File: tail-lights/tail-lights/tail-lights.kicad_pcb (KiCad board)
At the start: 2 copper layers, 145 x 115 mm, 106 parts, among them IC1 ATMEGA328P-AU, IC2 NCV8402ASTT1G, IC3 NCV8402ASTT1G, IC4 NCV8402ASTT1G, IC5 TPS62160DGKR, J1 Conn_01x01, J2 Conn_01x01, J3 Conn_01x06_Female, J4 Conn_01x04_Female, Y1 X322516MLB4SI

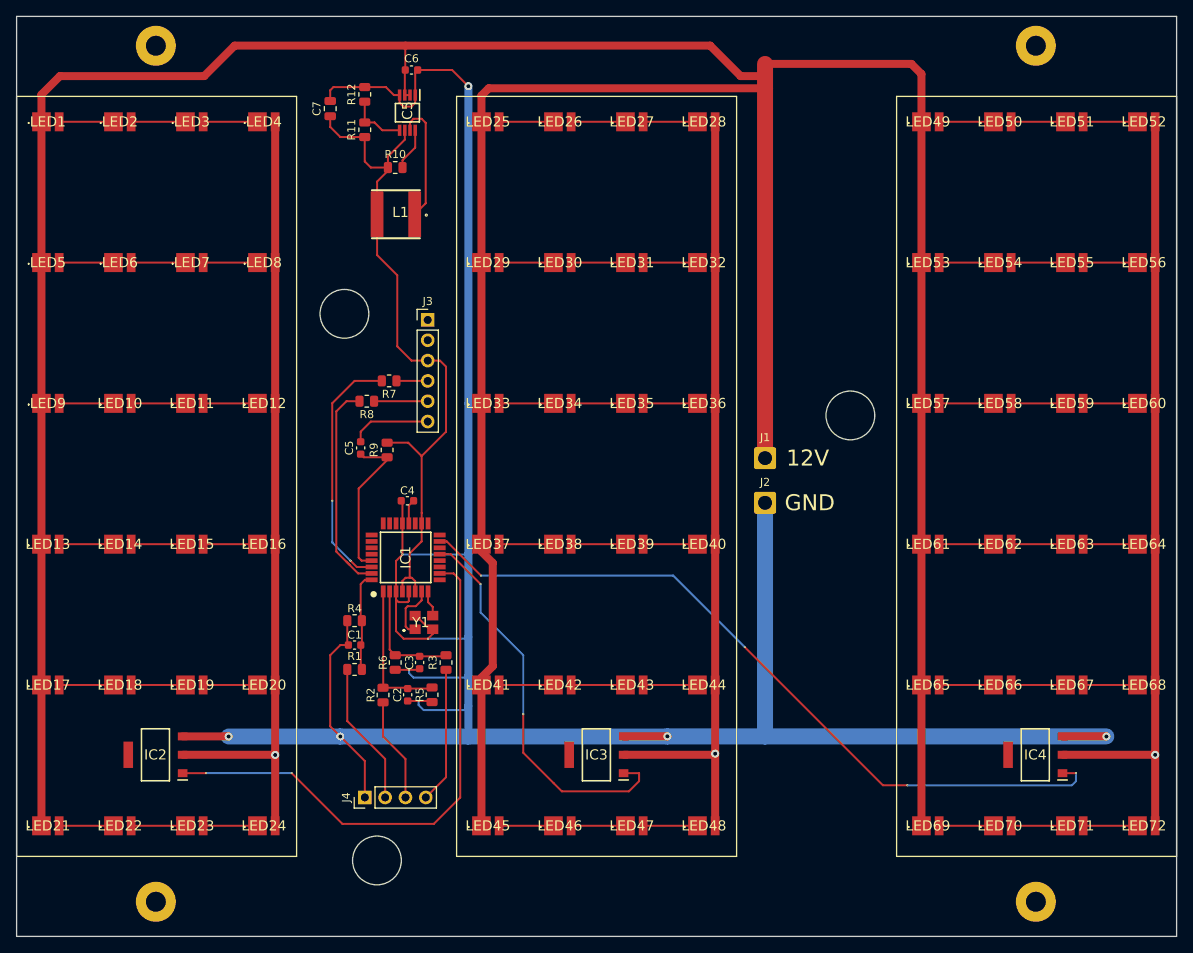
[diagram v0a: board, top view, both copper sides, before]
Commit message: Finalise tail-lights. Send off for fab
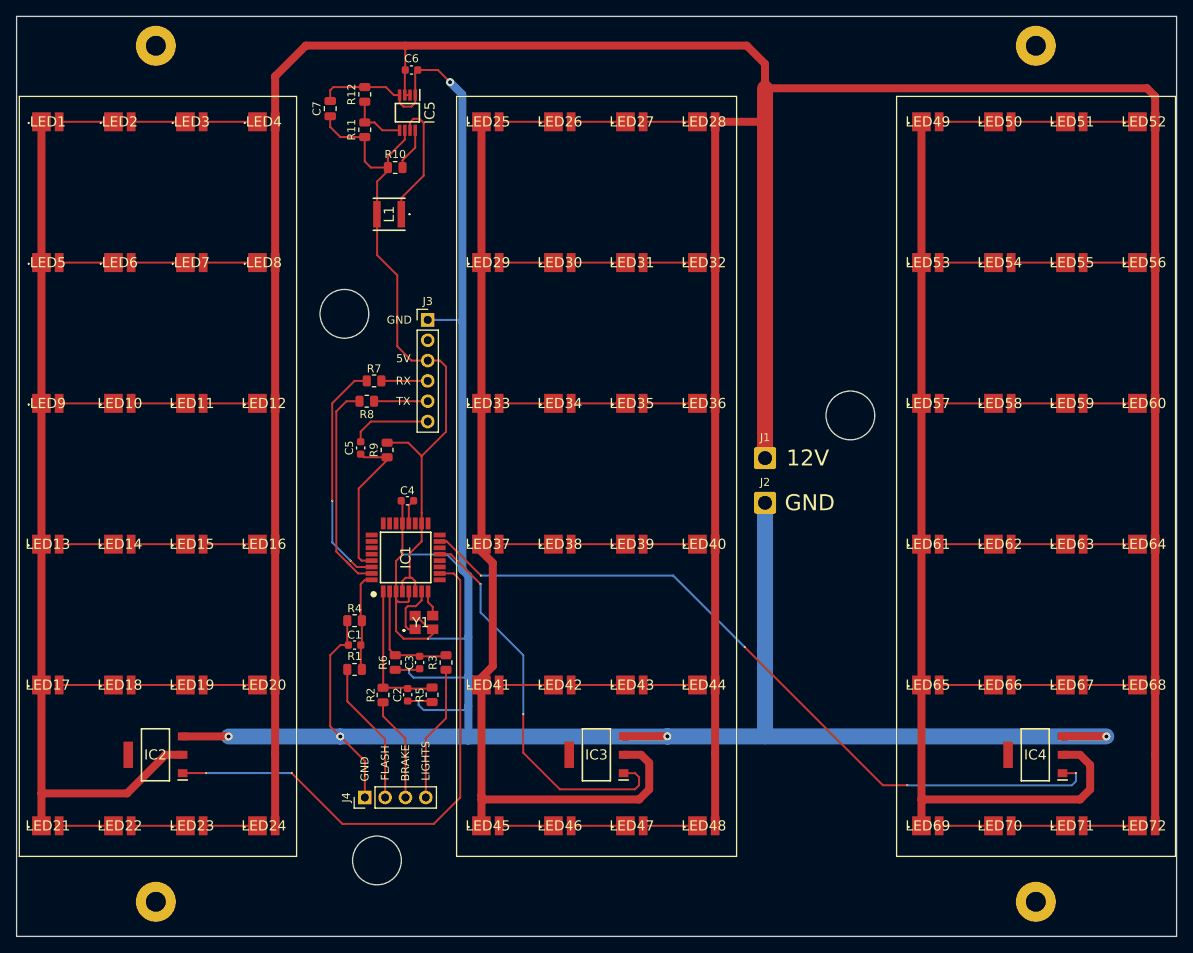
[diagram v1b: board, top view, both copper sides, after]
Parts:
- IC1: footprint Package_DIP:QFP80P900X900X120-32N -> Library:QFP80P900X900X120-32N
- IC2, IC3, IC4: footprint Symbol:SOT230P700X175-4N -> Library:SOT230P700X175-4N
- IC5: footprint Module:SOP65P490X110-8N -> Library:SOP65P490X110-8N
- L1: footprint Inductor_SMD:NR6028T220M -> Library:SMNR402022UH
- Y1: footprint Oscillator:X322516MLB4SI -> Library:X322516MLB4SI
- moved R7 1.88 mm to (71.8, 72.4)
- moved L1 0.85 mm to (73.7, 51.6), turned to 90 degrees
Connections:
- IC2 pad 2: Net-(LED12-Pad2) -> Net-(IC2-D_1)
- IC3 pad 2: Net-(LED28-Pad2) -> Net-(IC3-D_1)
- IC4 pad 2: Net-(LED52-Pad2) -> Net-(IC4-D_1)
- LED1 pad 1: 12V -> Net-(IC2-D_1)
- LED12 pad 2: Net-(LED12-Pad2) -> 12V
- LED13 pad 1: 12V -> Net-(IC2-D_1)
- LED16 pad 2: Net-(LED12-Pad2) -> 12V
- LED17 pad 1: 12V -> Net-(IC2-D_1)
- LED20 pad 2: Net-(LED12-Pad2) -> 12V
- LED21 pad 1: 12V -> Net-(IC2-D_1)
- LED24 pad 2: Net-(LED12-Pad2) -> 12V
- LED25 pad 1: 12V -> Net-(IC3-D_1)
- LED28 pad 2: Net-(LED28-Pad2) -> 12V
- LED29 pad 1: 12V -> Net-(IC3-D_1)
- LED32 pad 2: Net-(LED28-Pad2) -> 12V
- LED33 pad 1: 12V -> Net-(IC3-D_1)
- LED36 pad 2: Net-(LED28-Pad2) -> 12V
- LED37 pad 1: 12V -> Net-(IC3-D_1)
- LED4 pad 2: Net-(LED12-Pad2) -> 12V
- LED40 pad 2: Net-(LED28-Pad2) -> 12V
- LED41 pad 1: 12V -> Net-(IC3-D_1)
- LED44 pad 2: Net-(LED28-Pad2) -> 12V
- LED45 pad 1: 12V -> Net-(IC3-D_1)
- LED48 pad 2: Net-(LED28-Pad2) -> 12V
- LED49 pad 1: 12V -> Net-(IC4-D_1)
- LED5 pad 1: 12V -> Net-(IC2-D_1)
- LED52 pad 2: Net-(LED52-Pad2) -> 12V
- LED53 pad 1: 12V -> Net-(IC4-D_1)
- LED56 pad 2: Net-(LED52-Pad2) -> 12V
- LED57 pad 1: 12V -> Net-(IC4-D_1)
- LED60 pad 2: Net-(LED52-Pad2) -> 12V
- LED61 pad 1: 12V -> Net-(IC4-D_1)
- LED64 pad 2: Net-(LED52-Pad2) -> 12V
- LED65 pad 1: 12V -> Net-(IC4-D_1)
- LED68 pad 2: Net-(LED52-Pad2) -> 12V
- LED69 pad 1: 12V -> Net-(IC4-D_1)
- LED72 pad 2: Net-(LED52-Pad2) -> 12V
- LED8 pad 2: Net-(LED12-Pad2) -> 12V
- LED9 pad 1: 12V -> Net-(IC2-D_1)
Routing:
- net Net-(IC3-D_1): track 0.00 -> 117.6 mm
- net Net-(IC4-D_1): track 0.00 -> 116.6 mm
- net Net-(IC2-D_1): track 0.00 -> 107.6 mm
- net Net-(LED12-Pad2): track 99.7 -> 0.00 mm, vias 1 -> 0
- net Net-(LED52-Pad2): track 99.6 -> 0.00 mm, vias 1 -> 0
- net Net-(LED28-Pad2): track 99.5 -> 0.00 mm, vias 1 -> 0
- net 12V: track 484.7 -> 448.2 mm
- net GND: track 351.5 -> 355.6 mm
- net RX: track 3.91 -> 5.80 mm
- net Net-(IC1-PD0_(RXD/PCINT16)): track 31.0 -> 29.1 mm
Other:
- board text added: "5V"
- board text added: "BRAKE"
- board text added: "FLASH"
- board text added: "LIGHTS"
- board text added: "RX"
- board text added: "TX"

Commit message: Send tail lights v2 for fabrication
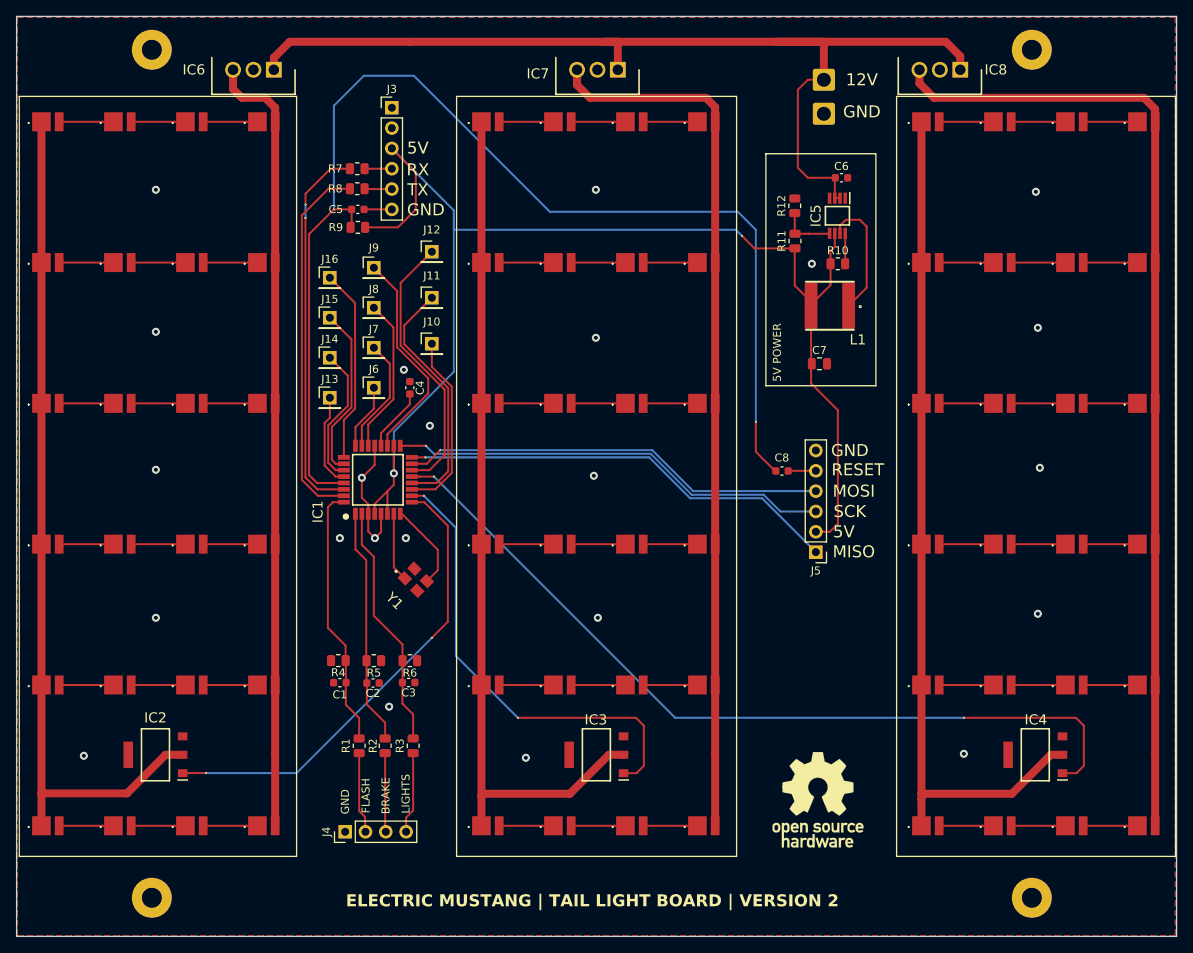
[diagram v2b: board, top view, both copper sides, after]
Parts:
- removed H4: MountingHole, MountingHole:MountingHole_2.5mm_Pad
- added C8: 0.1uF, Capacitor_SMD:C_0603_1608Metric, F.Cu at (122.8, 83.6)
- added H5: MountingHole_Pad, MountingHole:MountingHole_2.5mm_Pad, F.Cu at (44.0, 31.0)
- added IC6: L7812CV, Library:TO255P460X1020X2008-3P, F.Cu at (59.2, 33.5)
- added IC7: L7812CV, Library:TO255P460X1020X2008-3P, F.Cu at (102.2, 33.5)
- added IC8: L7812CV, Library:TO255P460X1020X2008-3P, F.Cu at (145.1, 33.5)
- added J10: Conn_01x01_Pin, Connector_PinHeader_2.54mm:PinHeader_1x01_P2.54mm_Vertical, F.Cu at (79.0, 67.8)
- added J11: Conn_01x01_Pin, Connector_PinHeader_2.54mm:PinHeader_1x01_P2.54mm_Vertical, F.Cu at (79.0, 62.0)
- added J12: Conn_01x01_Pin, Connector_PinHeader_2.54mm:PinHeader_1x01_P2.54mm_Vertical, F.Cu at (79.0, 56.2)
- added J13: Conn_01x01_Pin, Connector_PinHeader_2.54mm:PinHeader_1x01_P2.54mm_Vertical, F.Cu at (66.2, 74.5)
- added J14: Conn_01x01_Pin, Connector_PinHeader_2.54mm:PinHeader_1x01_P2.54mm_Vertical, F.Cu at (66.2, 69.5)
- added J15: Conn_01x01_Pin, Connector_PinHeader_2.54mm:PinHeader_1x01_P2.54mm_Vertical, F.Cu at (66.2, 64.5)
- added J16: Conn_01x01_Pin, Connector_PinHeader_2.54mm:PinHeader_1x01_P2.54mm_Vertical, F.Cu at (66.2, 59.5)
- added J5: Conn_01x06_Female, Connector_PinHeader_2.54mm:PinHeader_1x06_P2.54mm_Vertical, F.Cu at (127.0, 93.8)
- added J6: Conn_01x01_Pin, Connector_PinHeader_2.54mm:PinHeader_1x01_P2.54mm_Vertical, F.Cu at (71.8, 73.2)
- added J7: Conn_01x01_Pin, Connector_PinHeader_2.54mm:PinHeader_1x01_P2.54mm_Vertical, F.Cu at (71.8, 68.2)
- added J8: Conn_01x01_Pin, Connector_PinHeader_2.54mm:PinHeader_1x01_P2.54mm_Vertical, F.Cu at (71.8, 63.2)
- added J9: Conn_01x01_Pin, Connector_PinHeader_2.54mm:PinHeader_1x01_P2.54mm_Vertical, F.Cu at (71.8, 58.2)
- added REF**: OSHW-Logo_11.4x12mm_SilkScreen, Symbol:OSHW-Logo_11.4x12mm_SilkScreen, F.Cu at (127.2, 124.8)
- H1, H2, H3: value MountingHole -> MountingHole_Pad
- L1: footprint Library:SMNR402022UH -> Library:NR6028T220M
- moved H2 153.5 mm to (44.0, 137.0)
- moved H1 109.5 mm to (154.0, 31.0)
- moved H3 109.5 mm to (154.0, 137.0)
- moved C7 69.0 mm to (127.5, 70.2), turned to 0 degrees
- moved R10 56.6 mm to (129.8, 57.8)
- moved L1 56.3 mm to (128.8, 63.0), turned to 180 degrees
- moved R11 55.5 mm to (124.4, 54.9)
- moved R12 55.5 mm to (124.4, 50.5)
- moved C6 55.4 mm to (130.2, 47.0)
- moved IC5 55.3 mm to (129.7, 51.8)
- moved J2 49.2 mm to (128.0, 39.0)
- moved J1 47.9 mm to (128.0, 34.8)
- moved C5 29.8 mm to (69.8, 51.0), turned to 0 degrees
- moved R9 28.1 mm to (69.8, 53.2), turned to 0 degrees
- moved J3 26.9 mm to (74.0, 38.2)
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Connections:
- H1 pad 1: (no net) -> GND
- H2 pad 1: (no net) -> GND
- H3 pad 1: (no net) -> GND
- IC1 pad 10: BLOCK_1_SIGNAL -> BLOCK_2_SIGNAL
- IC1 pad 11: unconnected-(IC1-(PCINT23/AIN1)_PD7-Pad11) -> Net-(IC1-(PCINT23/AIN1)_PD7)
- IC1 pad 12: unconnected-(IC1-(PCINT0/CLKO/ICP1)_PB0-Pad12) -> Net-(IC1-(PCINT0/CLKO/ICP1)_PB0)
- IC1 pad 13: BLOCK_2_SIGNAL -> BLOCK_3_SIGNAL
- IC1 pad 14: unconnected-(IC1-(PCINT2/SS/OC1B)_PB2-Pad14) -> Net-(IC1-(PCINT2/SS/OC1B)_PB2)
- IC1 pad 15: BLOCK_3_SIGNAL -> MOSI
- IC1 pad 16: unconnected-(IC1-(PCINT4/MISO)_PB4-Pad16) -> MISO
- IC1 pad 17: unconnected-(IC1-PB5_(SCK/PCINT5)-Pad17) -> SCK
- IC1 pad 19: unconnected-(IC1-ADC6-Pad19) -> Net-(IC1-ADC6)
- IC1 pad 22: unconnected-(IC1-ADC7-Pad22) -> Net-(IC1-ADC7)
- IC1 pad 23: unconnected-(IC1-PC0_(ADC0/PCINT8)-Pad23) -> Net-(IC1-PC0_(ADC0/PCINT8))
- IC1 pad 24: unconnected-(IC1-PC1_(ADC1/PCINT9)-Pad24) -> Net-(IC1-PC1_(ADC1/PCINT9))
- IC1 pad 25: unconnected-(IC1-PC2_(ADC2/PCINT10)-Pad25) -> Net-(IC1-PC2_(ADC2/PCINT10))
- IC1 pad 26: unconnected-(IC1-PC3_(ADC3/PCINT11)-Pad26) -> Net-(IC1-PC3_(ADC3/PCINT11))
- IC1 pad 27: unconnected-(IC1-PC4_(ADC4/SDA/PCINT12)-Pad27) -> Net-(IC1-PC4_(ADC4/SDA/PCINT12))
- IC1 pad 28: unconnected-(IC1-PC5_(ADC5/SCL/PCINT13)-Pad28) -> Net-(IC1-PC5_(ADC5/SCL/PCINT13))
- IC1 pad 9: unconnected-(IC1-(PCINT21/OC0B/T1)_PD5-Pad9) -> BLOCK_1_SIGNAL
- LED12 pad 2: 12V -> Net-(IC6-OUTPUT)
- LED16 pad 2: 12V -> Net-(IC6-OUTPUT)
- LED20 pad 2: 12V -> Net-(IC6-OUTPUT)
- LED24 pad 2: 12V -> Net-(IC6-OUTPUT)
- LED28 pad 2: 12V -> Net-(IC7-OUTPUT)
- LED32 pad 2: 12V -> Net-(IC7-OUTPUT)
- LED36 pad 2: 12V -> Net-(IC7-OUTPUT)
- LED4 pad 2: 12V -> Net-(IC6-OUTPUT)
- LED40 pad 2: 12V -> Net-(IC7-OUTPUT)
- LED44 pad 2: 12V -> Net-(IC7-OUTPUT)
- LED48 pad 2: 12V -> Net-(IC7-OUTPUT)
- LED52 pad 2: 12V -> Net-(IC8-OUTPUT)
- LED56 pad 2: 12V -> Net-(IC8-OUTPUT)
- LED60 pad 2: 12V -> Net-(IC8-OUTPUT)
- LED64 pad 2: 12V -> Net-(IC8-OUTPUT)
- LED68 pad 2: 12V -> Net-(IC8-OUTPUT)
- LED72 pad 2: 12V -> Net-(IC8-OUTPUT)
- LED8 pad 2: 12V -> Net-(IC6-OUTPUT)
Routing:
- net GND: track 355.6 -> 16.2 mm, vias 9 -> 23
- net 12V: track 448.2 -> 128.5 mm
- net RESET: track 19.3 -> 150.2 mm, vias 0 -> 2
- net Net-(IC8-OUTPUT): track 0.00 -> 122.1 mm
- net Net-(IC7-OUTPUT): track 0.00 -> 110.1 mm
- net Net-(IC6-OUTPUT): track 0.00 -> 98.4 mm
- net 5V: track 86.9 -> 171.6 mm, vias 0 -> 2
- net MISO: track 0.00 -> 55.4 mm, vias 0 -> 1
- net SCK: track 0.00 -> 55.4 mm, vias 0 -> 1
- net MOSI: track 0.00 -> 53.3 mm, vias 0 -> 1
- net Net-(IC1-(PCINT2/SS/OC1B)_PB2): track 0.00 -> 34.2 mm
- net Net-(IC1-(PCINT0/CLKO/ICP1)_PB0): track 0.00 -> 30.6 mm
- net Net-(IC1-ADC6): track 0.00 -> 27.2 mm
- net Net-(IC1-PC2_(ADC2/PCINT10)): track 0.00 -> 24.3 mm
- net Net-(IC1-(PCINT23/AIN1)_PD7): track 0.00 -> 23.0 mm
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- added copper zone on B.Cu, net GND
- added copper zone on F.Cu, net GND
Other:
- outline, holes or cut-outs redrawn
- board text added: "5V POWER"
- board text added: "ELECTRIC MUSTANG | TAIL LIGHT BOARD | VERSION 2"
- board text added: "MISO"
- board text added: "MOSI"
- board text added: "RESET"
- board text added: "SCK"
